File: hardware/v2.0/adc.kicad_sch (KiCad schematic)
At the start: 12 parts, among them IC2 LTC2256CUJ-12#PBF, U1 ECP5U-25F-CABGA256, Y2 SG-8018CG 50.000000MHz

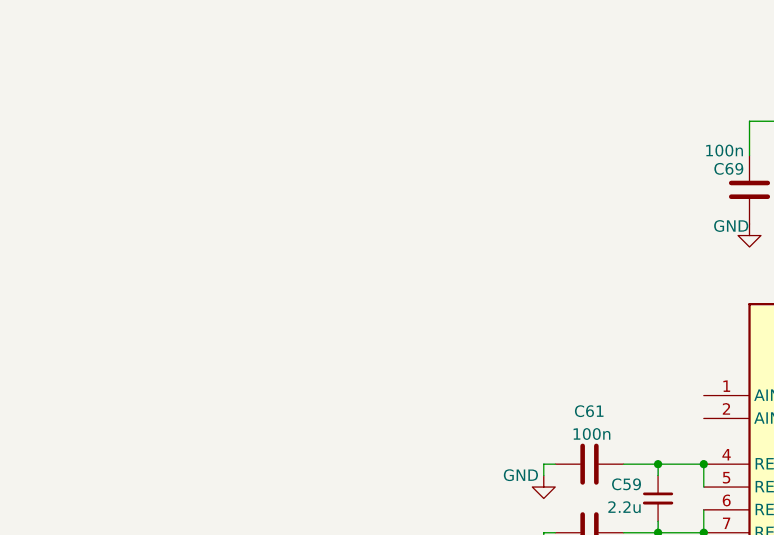
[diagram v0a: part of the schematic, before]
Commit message: LEDs update for IC
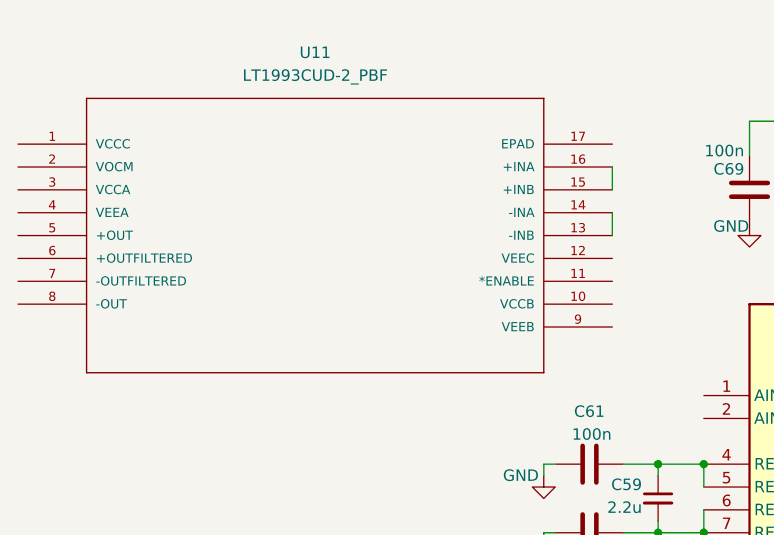
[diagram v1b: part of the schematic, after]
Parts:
- added U11: LT1993CUD-2_PBF, LT1993CUD_2_PBF:QFN-16_UD, symbol LT1993CUD-2_PBF:LT1993CUD-2_PBF
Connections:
- new net: U11.13 (-INB), U11.14 (-INA)
- new net: U11.15 (+INB), U11.16 (+INA)
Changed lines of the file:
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@@
+	(wire
+		(pts
+			(xy 87.63 35.56) (xy 87.63 38.1)
+		)
+		(stroke
+			(width 0)
+			(type default)
+		)
+	)
 	(wire
 		(pts
@@
 		(pts
 			(xy 138.43 62.23) (xy 157.48 62.23)
+		)
+		(stroke
+			(width 0)
+			(type default)
+		)
+	)
+	(wire
+		(pts
+			(xy 87.63 40.64) (xy 87.63 43.18)
 		)
 		(stroke
@@
 					(unit 1)
 				)
+			)
+		)
+	)
+	(symbol
+		(lib_id "LT1993CUD-2_PBF:LT1993CUD-2_PBF")
+		(at 21.59 33.02 0)
+		(unit 1)
+		(exclude_from_sim no)
+		(in_bom yes)
+		(on_board yes)
+		(dnp no)
+		(fields_autoplaced yes)
+		(property "Reference" "U11"
+			(at 54.61 22.86 0)
+			(effects
+				(font
+					(size 1.27 1.27)
+				)
+			)
+		)
+		(property "Value" "LT1993CUD-2_PBF"
+			(at 54.61 25.4 0)
+			(effects
+				(font
+					(size 1.27 1.27)
+				)
+			)
+		)
+		(property "Footprint" "LT1993CUD_2_PBF:QFN-16_UD"
+			(at 21.59 33.02 0)
+			(effects
+				(font
+					(size 1.27 1.27)
+				)
+				(justify bottom)
+				(hide yes)
+			)
+		)
+		(property "Datasheet" ""
+			(at 21.59 33.02 0)
+			(effects
+				(font
+					(size 1.27 1.27)
+				)
+				(hide yes)
+			)
+		)
+		(property "Description" ""
+			(at 21.59 33.02 0)
+			(effects
+				(font
+					(size 1.27 1.27)
+				)
+				(hide yes)
+			)
+		)
+		(property "VENDOR" "Linear Technology"
+			(at 21.59 33.02 0)
+			(effects
+				(font
+					(size 1.27 1.27)
+				)
+				(justify bottom)
+				(hide yes)
+			)
+		)
+		(property "MANUFACTURER_PART_NUMBER" "lt1993cud2"
+			(at 21.59 33.02 0)
+			(effects
+				(font
+					(size 1.27 1.27)
+				)
+				(justify bottom)
+				(hide yes)
+			)
+		)
+		(pin "7"
+		)
+		(pin "12"
+		)
+		(pin "17"
+		)
+		(pin "16"
+		)
+		(pin "8"
+		)
+		(pin "15"
+		)
+		(pin "1"
+		)
+		(pin "3"
+		)
+		(pin "2"
+		)
+		(pin "9"
+		)
+		(pin "4"
+		)
+		(pin "14"
+		)
+		(pin "13"
+		)
+		(pin "5"
+		)
+		(pin "11"
+		)
+		(pin "6"
+		)
+		(pin "10"
+		)
+		(instances
+			(project ""
+				(path "/f88da08e-cf42-4d03-a08f-3f602fe6658d/b5a9aa02-311b-4a9a-a7d4-646f15cdd9c2"
+					(reference "U11")
+					(unit 1)
+				)

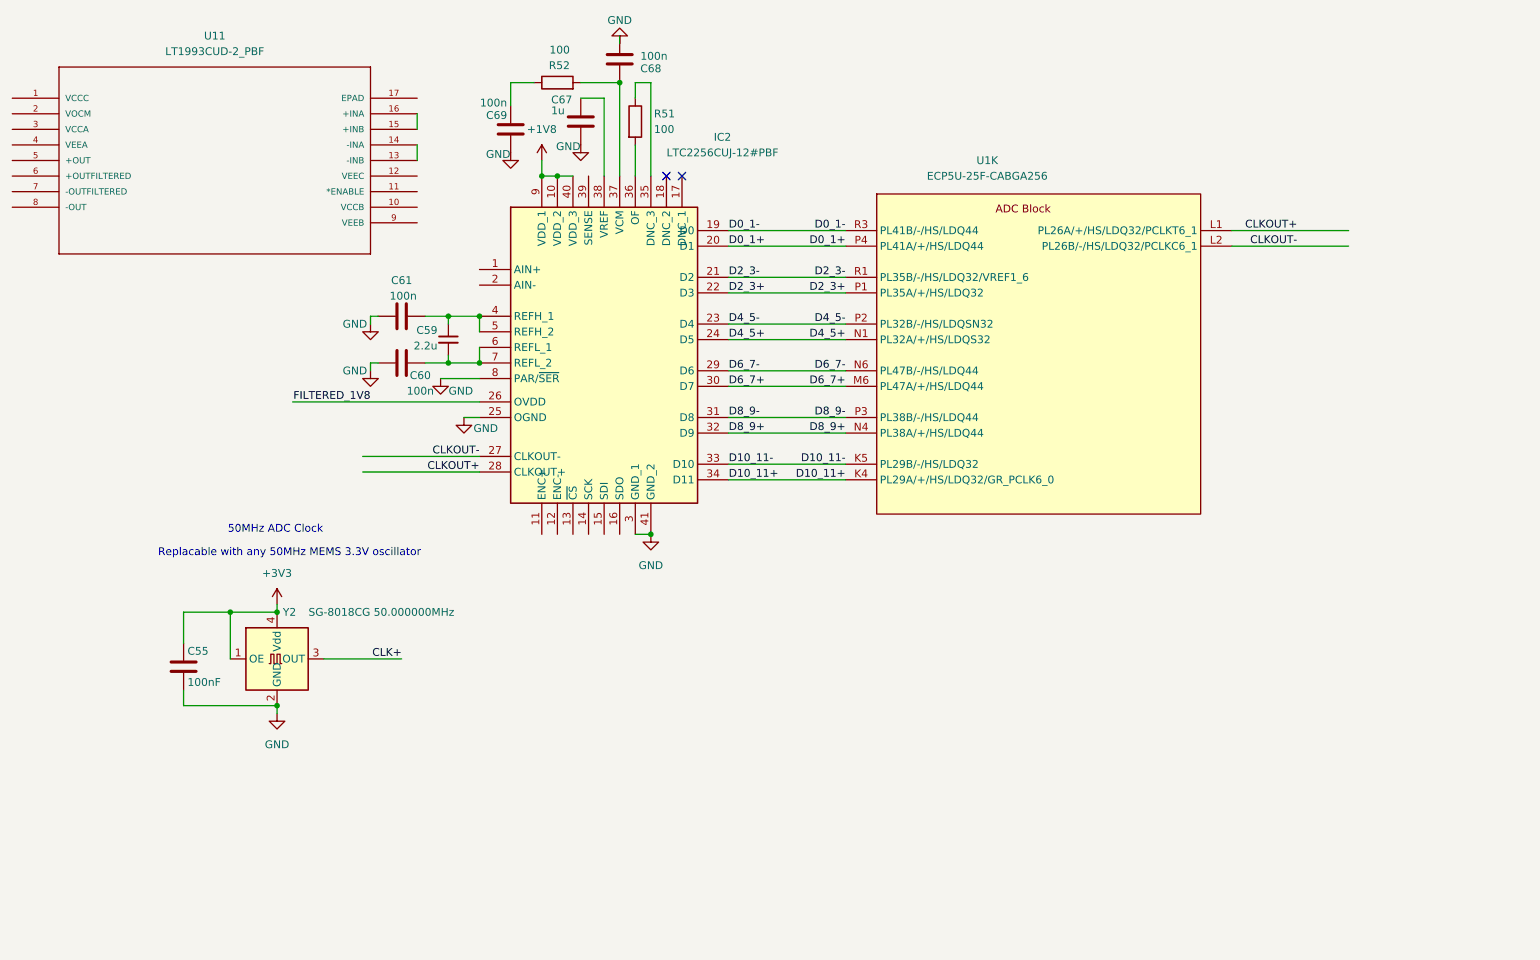
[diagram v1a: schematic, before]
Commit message: ADC driver enable pin
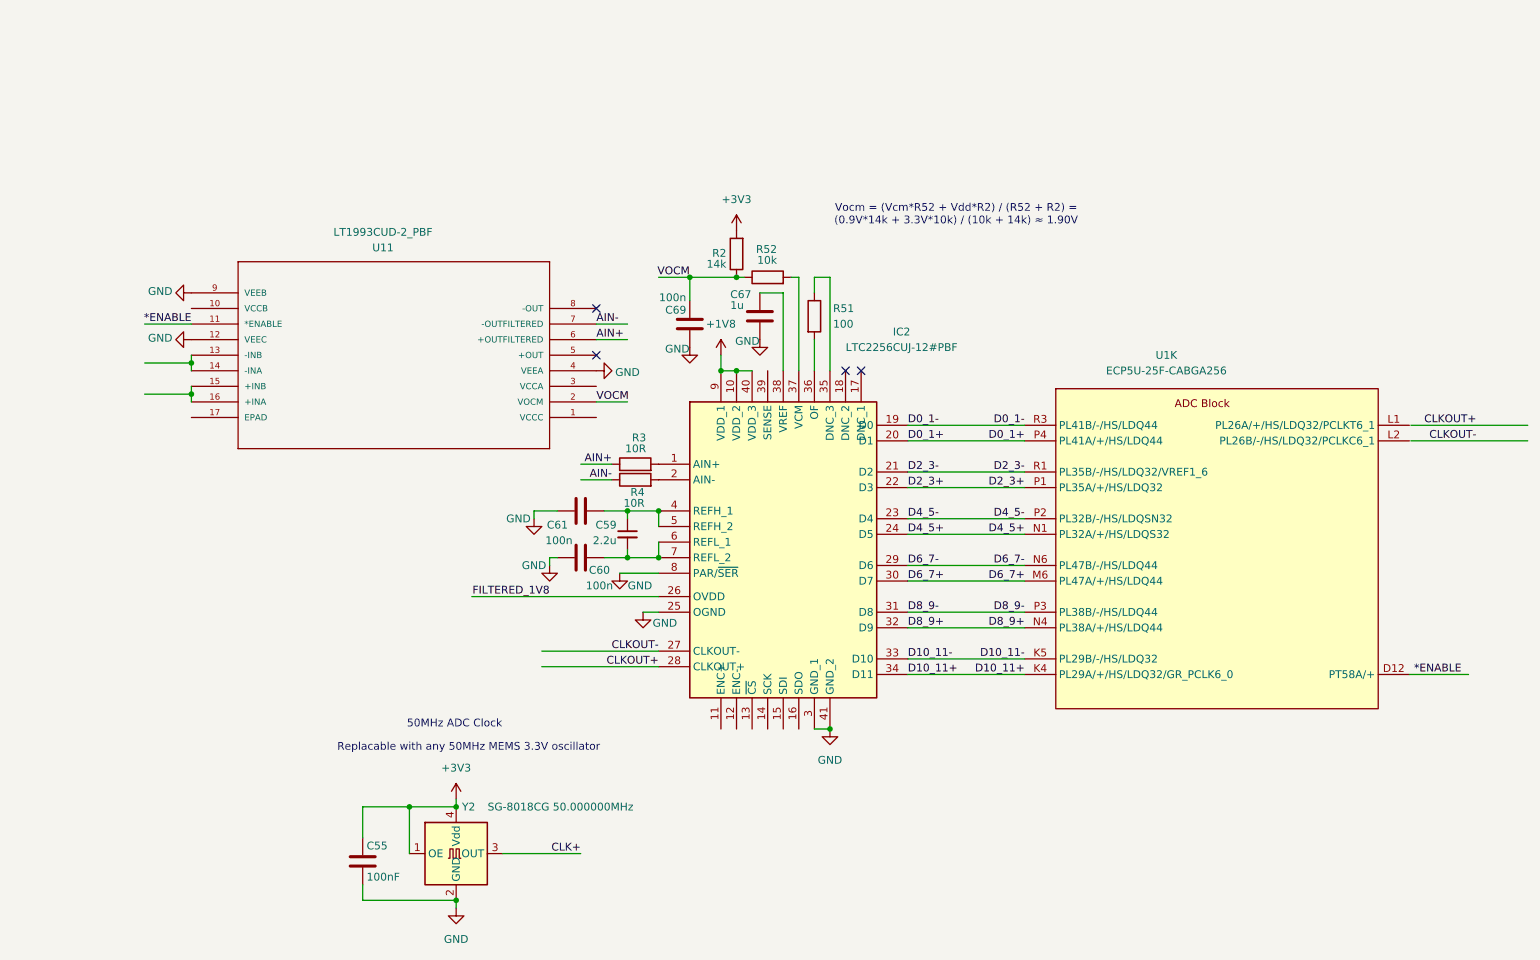
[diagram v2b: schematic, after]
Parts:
- removed C68: 100n, Capacitor_SMD:C_0402_1005Metric, symbol Device:C
- added R2: 14k, Resistor_SMD:R_0402_1005Metric, symbol Device:R
- added R3, R4: 10R, Resistor_SMD:R_0402_1005Metric, symbol Device:R
- R52: value 100 -> 10k; LCSC Link https://www.lcsc.com/product-detail/C25076.html -> https://www.lcsc.com/product-detail/C25744.html; LCSC Part # C25076 -> C25744; Manufactuer Part Number 0402WGF1000TCE -> 0402WGF1002TCE
- U11: footprint LT1993CUD_2_PBF:QFN-16_UD -> LT1993CUD-2_PBF:QFN-16_UD
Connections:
- net +3V3: now also R2.2
- net CLKOUT+: no longer U1.L1 (PL26A/+/HS/LDQ32/PCLKT6_1)
- net CLKOUT-: no longer U1.L2 (PL26B/-/HS/LDQ32/PCLKC6_1)
- net GND: now also U11.12 (VEEC), U11.4 (VEEA), U11.9 (VEEB)
- net VOCM: now reaches C69.1, R52.1
- net VOCM: now also U11.2 (VOCM), R2.1
- net *ENABLE: now reaches U11.11 (*ENABLE)
- net *ENABLE: now also U1.D12 (PT58A/+)
- net AIN+: now reaches U11.6 (+OUTFILTERED)
- net AIN+: now also R3.1
- net AIN-: now reaches U11.7 (-OUTFILTERED)
- net AIN-: now also R4.1
- net at IC2.1 (AIN+): now also R3.2
- net at IC2.2 (AIN-): now also R4.2
- no-connect marks 2 -> 4
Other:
- note added: "Vocm = (Vcm*R52 + Vdd*R2) / (R52 + R2) = (0.9V*14k + 3.3V*10k) / (10k + 14k) ≈ 1.90V"
- moved on the sheet: C55, C59, C60, C61, C67, C69, IC2, R51, R52, U11, Y2

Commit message: ADC SPI
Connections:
- net CLKOUT+: now also U1.L1 (PL26A/+/HS/LDQ32/PCLKT6_1)
- net CLKOUT-: now also U1.L2 (PL26B/-/HS/LDQ32/PCLKC6_1)
- net ~{CS}: now reaches IC2.13 (~{CS})
- net ~{CS}: now also U1.D13 (PT62A/+)
- net SCK: now reaches IC2.14 (SCK)
- net SCK: now also U1.C13 (PT60B/-)
- net SDI: now reaches IC2.15 (SDI)
- net SDI: now also U1.E12 (PT58B/-)
- net SDO: now reaches IC2.16 (SDO)
- net SDO: now also U1.E13 (PT62B/-)

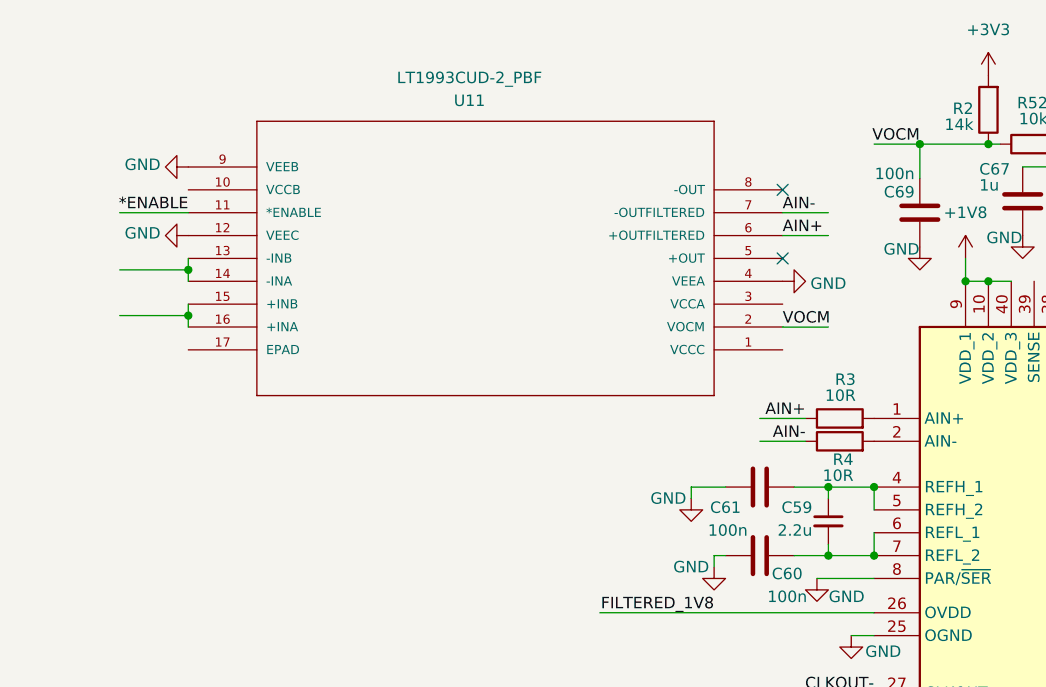
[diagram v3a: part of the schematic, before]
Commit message: ADC input driver power
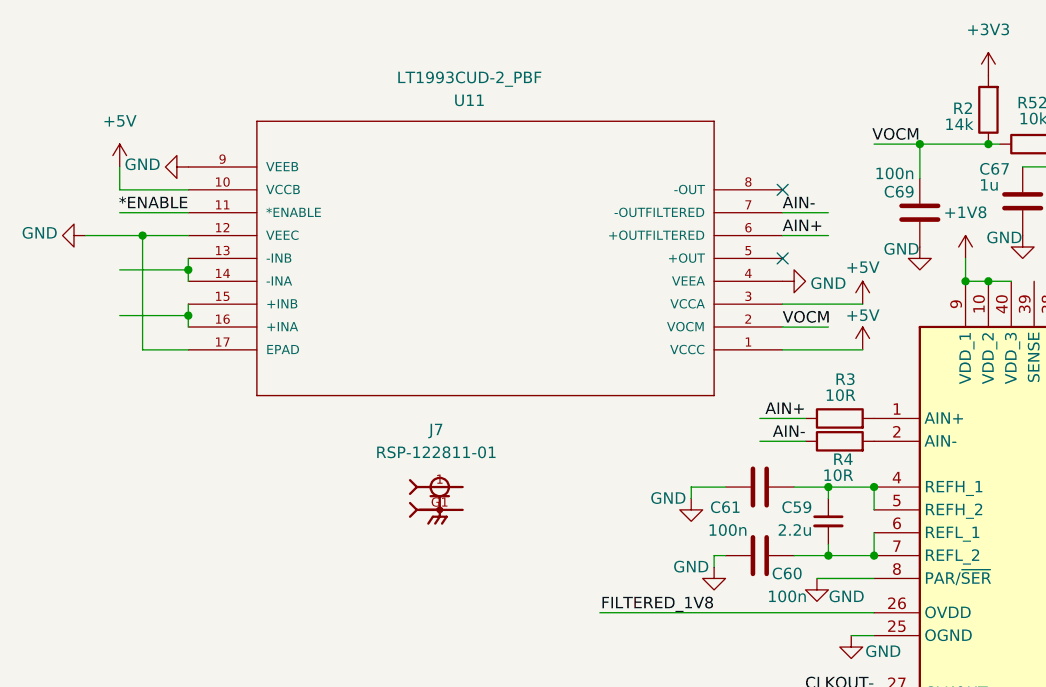
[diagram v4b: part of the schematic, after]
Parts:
- added J7: RSP-122811-01, RSP-122811-01:SAMTEC_RSP-122811-01, symbol RSP-122811-01:RSP-122811-01
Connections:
- net GND: now also U11.17 (EPAD)
- net +5V: now reaches U11.1 (VCCC)
- net +5V: now also U11.10 (VCCB), U11.3 (VCCA)
- new net: J7.G1, J7.G2

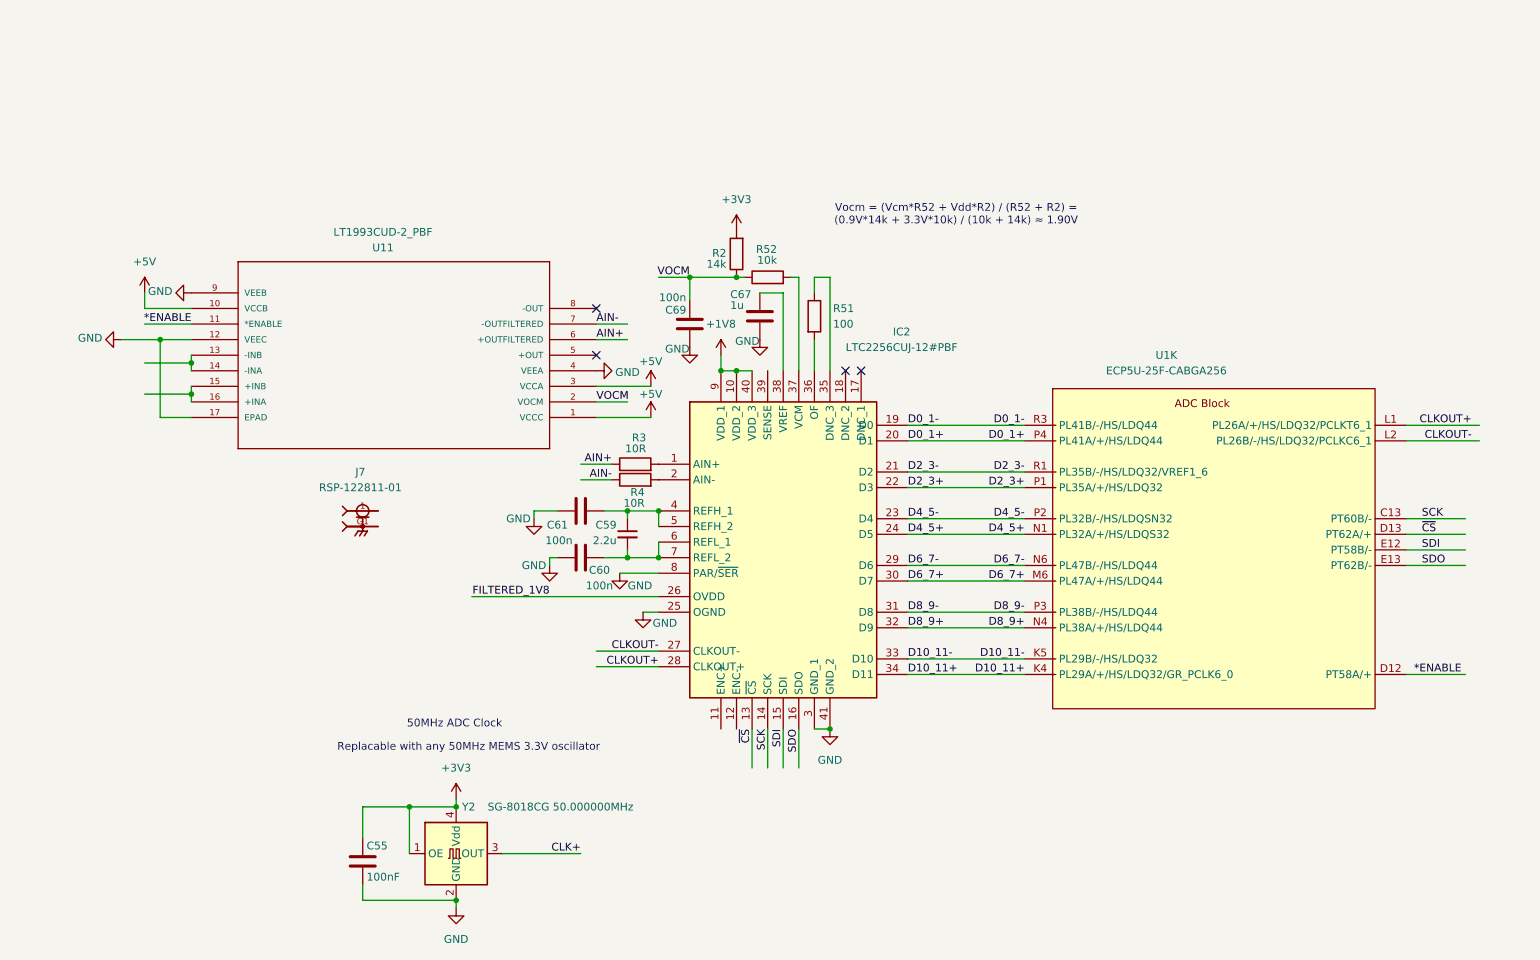
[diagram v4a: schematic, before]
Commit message: ADC sense
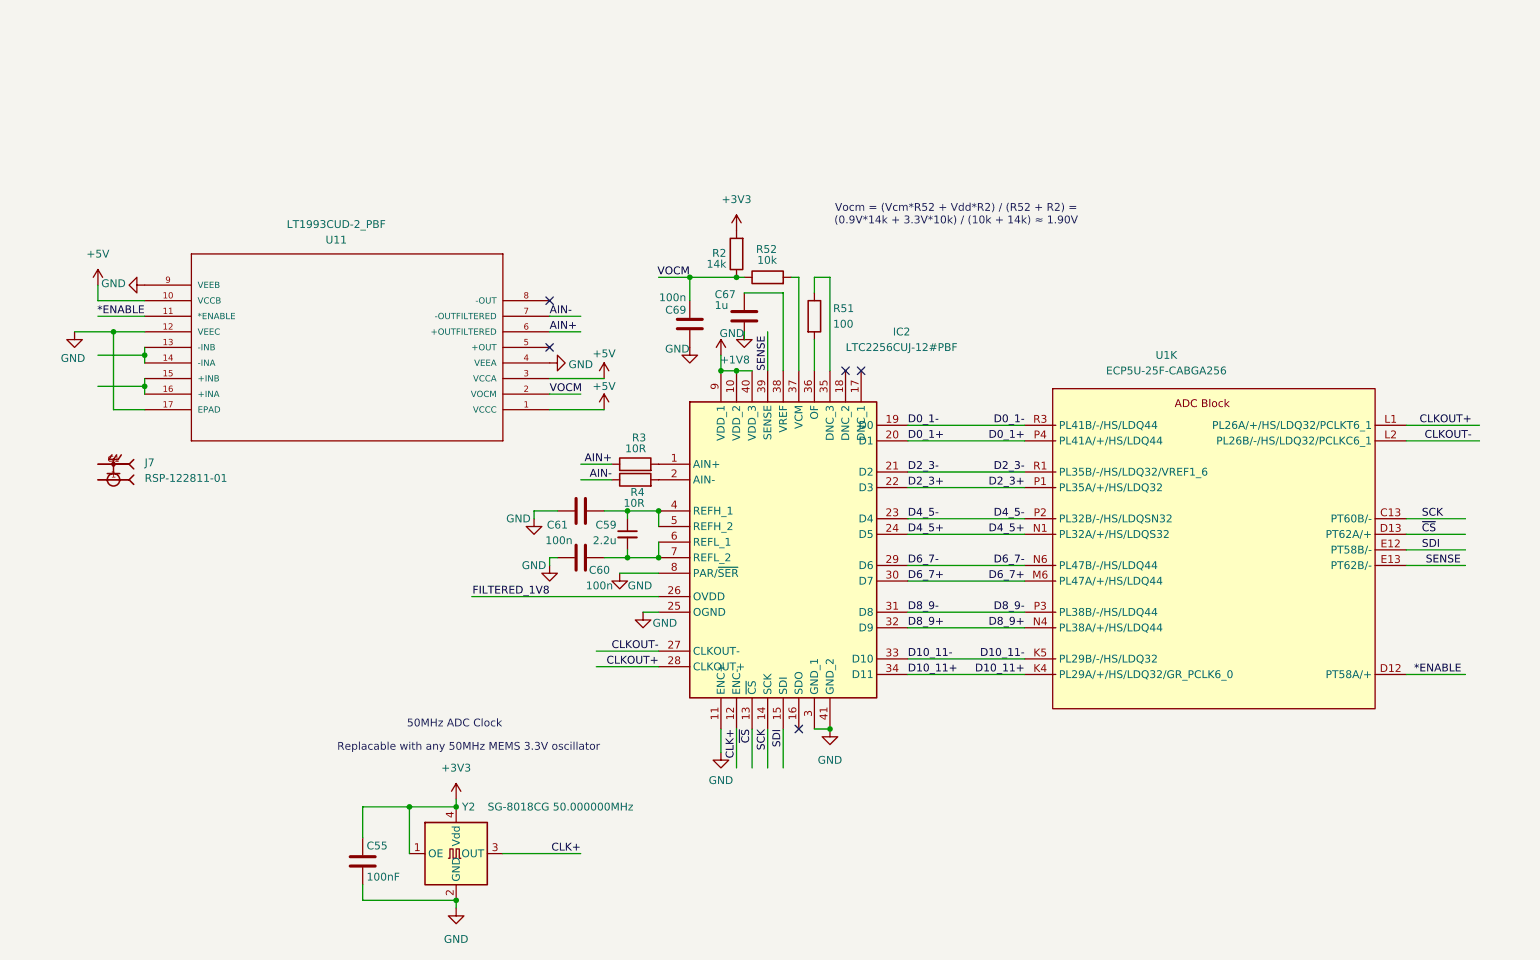
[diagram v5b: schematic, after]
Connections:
- net CLK+: now also IC2.12 (ENC-)
- net GND: now also IC2.11 (ENC+)
- net SENSE: now reaches IC2.39 (SENSE)
- net SENSE: now also U1.E13 (PT62B/-)
- net SDO: no longer names the net of IC2.16 (SDO)
- net SDO: no longer U1.E13 (PT62B/-)
- no-connect marks 4 -> 5
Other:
- moved on the sheet: C67, J7, U11

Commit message: DRC almost pass
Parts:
- added C74: 1u, Capacitor_SMD:C_0402_1005Metric, symbol Device:C
- added R5: 1k, Resistor_SMD:R_0402_1005Metric, symbol Device:R
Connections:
- net +1V8: now also R5.2
- net GND: now also C74.2
- net SENSE: now also C74.1, R5.1
- net VOCM: now also R52.2; no longer R52.1
- net at IC2.37 (VCM): now also R52.1; no longer R52.2
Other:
- moved on the sheet: C67, C69, R2, R52
